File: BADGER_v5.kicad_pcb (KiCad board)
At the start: 2 copper layers, 101.6 x 78.7 mm, 116 parts, among them J4 ZIF-40-0.5, P1 PCB, P2 ISP, P3 FTDI, P4 C3SB, P5 JST_3V7, P6 V_IN, P7 UUSB_B, Q1 DMG2301U-7, Q2 2N7002KW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

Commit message: changed to v4.1 and added Logo
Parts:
- added G***: LOGO, Wyolum_logo_4, F.Cu at (116.9, 73.1)
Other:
- board text added: "BADGEr_v4.1"
- board text removed: "BADGEr _ v5"
- board text removed: "v 5"

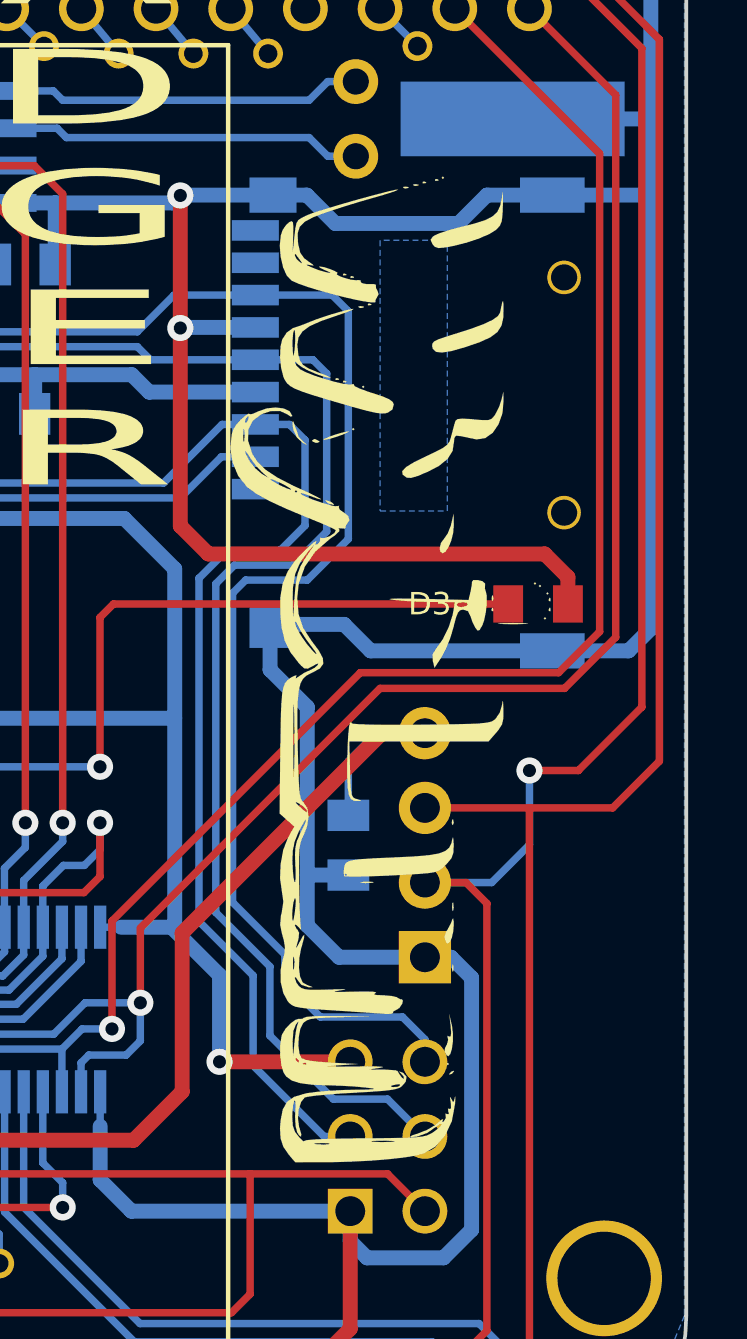
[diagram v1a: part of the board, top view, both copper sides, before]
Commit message: modified WyoLum logo on front legend
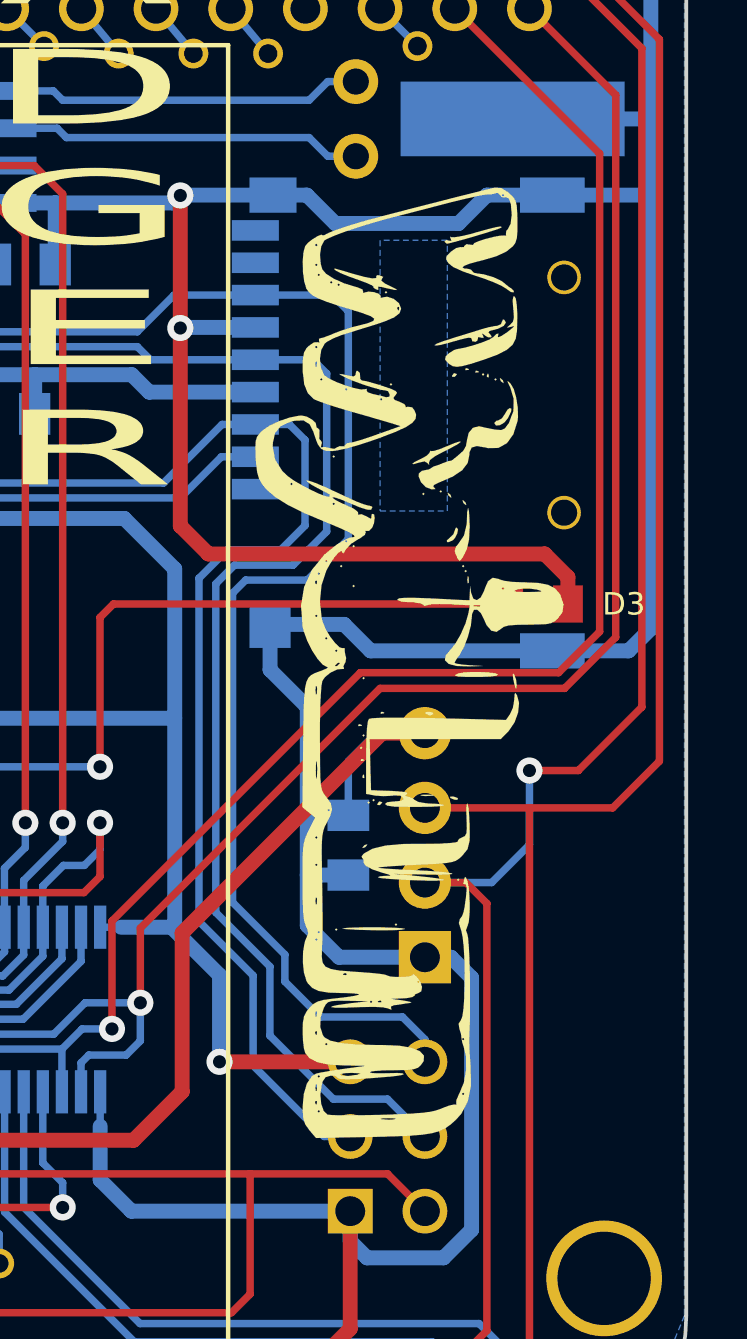
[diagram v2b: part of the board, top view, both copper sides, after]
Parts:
- removed the G*** at (116.9, 73.1)
- added G***: LOGO, wyolum_logo_1, F.Cu at (117.7, 73.1)
